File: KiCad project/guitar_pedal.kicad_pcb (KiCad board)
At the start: 2 copper layers, 7 parts, among them J1 NMJ6HCD2, J2 NMJ6HCD2, J3 AVR-ISP-6, SW2 SWITCH_3PDT, U1 ATmega1284-P, U2 L7805

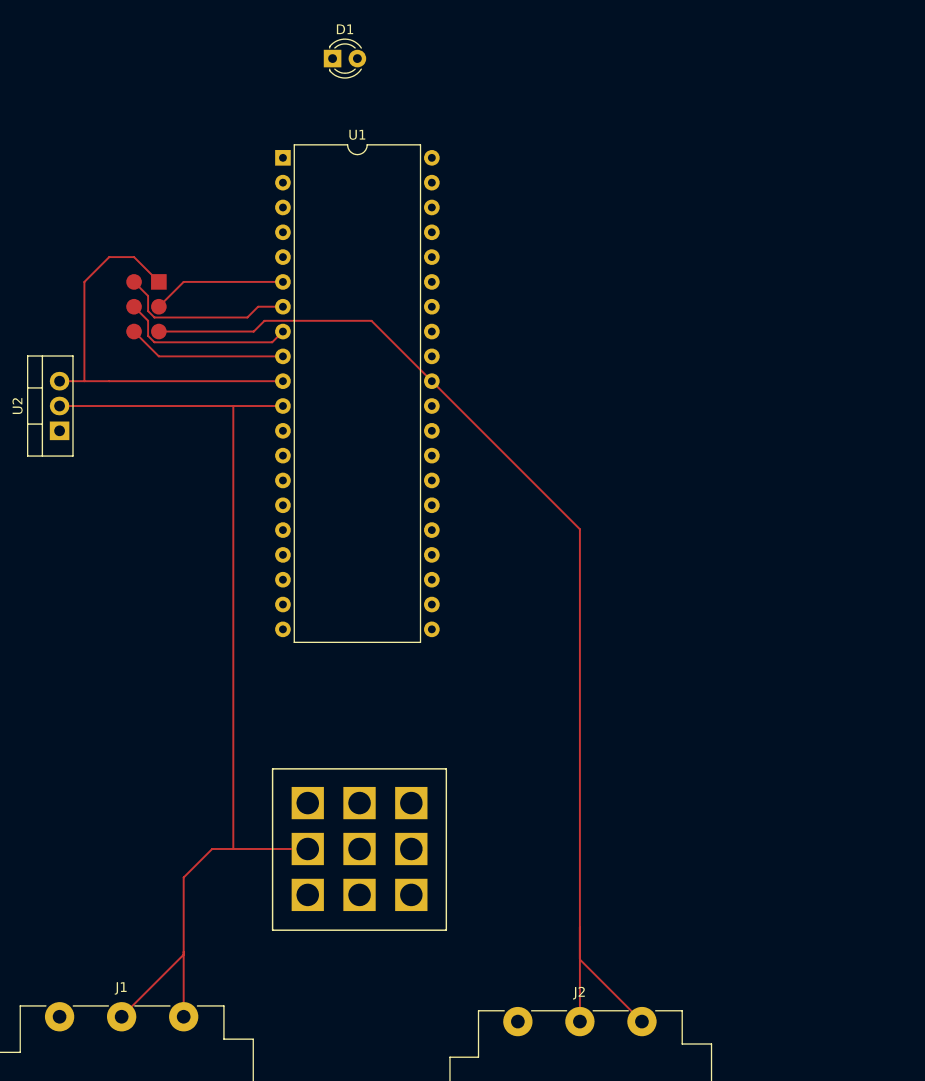
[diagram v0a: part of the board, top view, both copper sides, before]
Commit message: Updated components with footprints, added to PCB
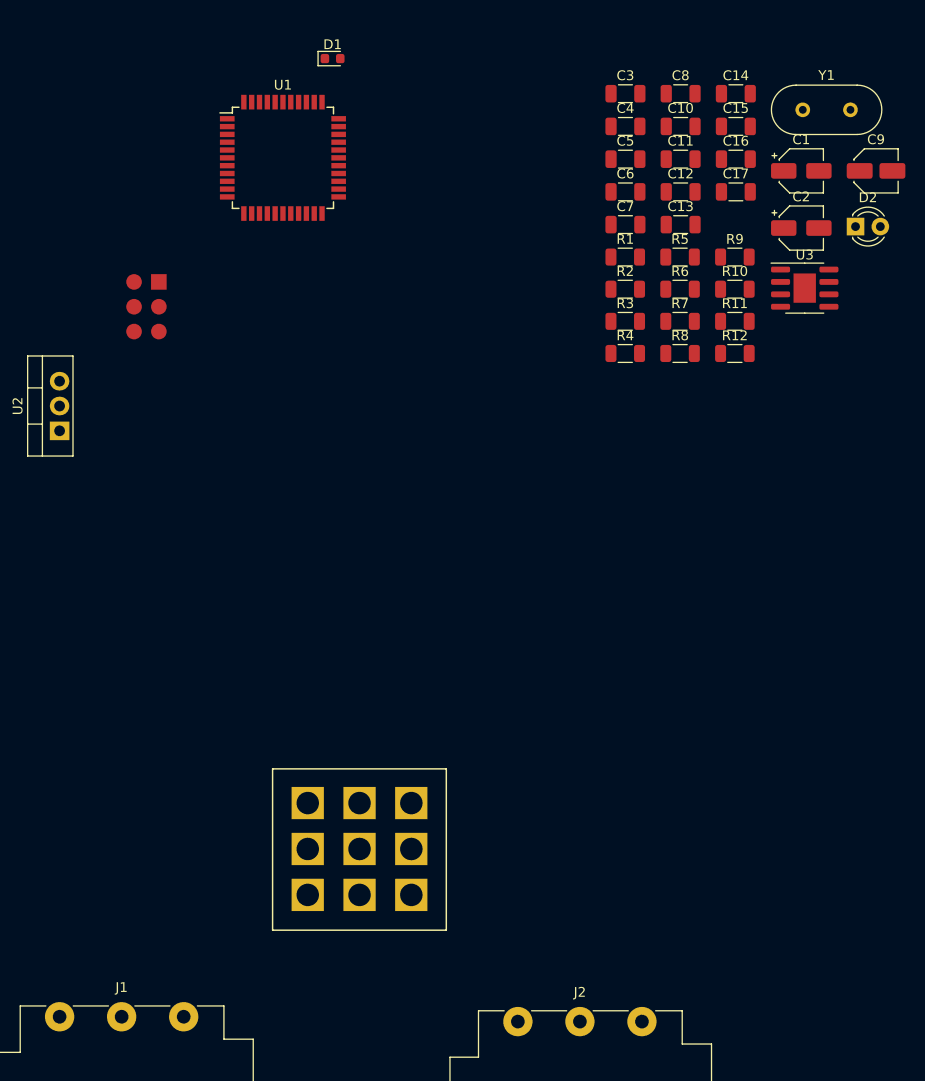
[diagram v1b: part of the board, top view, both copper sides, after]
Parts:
- added C1: 10u, Capacitor_SMD:CP_Elec_4x5.4, F.Cu at (103.9, 44.5)
- added C10: 6.8n, Capacitor_SMD:C_1206_3216Metric, F.Cu at (91.5, 40.0)
- added C11: 6.8n, Capacitor_SMD:C_1206_3216Metric, F.Cu at (91.5, 43.3)
- added C12: 6.8n, Capacitor_SMD:C_1206_3216Metric, F.Cu at (91.5, 46.7)
- added C13: 100n, Capacitor_SMD:C_1206_3216Metric, F.Cu at (91.5, 50.0)
- added C14: 6.8n, Capacitor_SMD:C_1206_3216Metric, F.Cu at (97.2, 36.6)
- added C15: 0.1u, Capacitor_SMD:C_1206_3216Metric, F.Cu at (97.2, 40.0)
- added C16: 0.1u, Capacitor_SMD:C_1206_3216Metric, F.Cu at (97.2, 43.3)
- added C17: 0.1u, Capacitor_SMD:C_1206_3216Metric, F.Cu at (97.2, 46.7)
- added C2: 10u, Capacitor_SMD:CP_Elec_4x5.4, F.Cu at (103.9, 50.4)
- added C3: 0.33u, Capacitor_SMD:C_1206_3216Metric, F.Cu at (85.9, 36.6)
- added C4: 0.1u, Capacitor_SMD:C_1206_3216Metric, F.Cu at (85.9, 40.0)
- added C5: 22p, Capacitor_SMD:C_1206_3216Metric, F.Cu at (85.9, 43.3)
- added C6: 22p, Capacitor_SMD:C_1206_3216Metric, F.Cu at (85.9, 46.7)
- added C7: 0.1u, Capacitor_SMD:C_1206_3216Metric, F.Cu at (85.9, 50.0)
- added C8: 270p, Capacitor_SMD:C_1206_3216Metric, F.Cu at (91.5, 36.6)
- added C9: 1u, Capacitor_SMD:C_Elec_4x5.4, F.Cu at (111.5, 44.5)
- added D2: GREEN LED, LED_THT:LED_D3.0mm, F.Cu at (109.4, 50.2)
- added R1: 330, Resistor_SMD:R_1206_3216Metric, F.Cu at (85.8, 53.3)
- added R10: 4.7k, Resistor_SMD:R_1206_3216Metric, F.Cu at (97.1, 56.6)
- added R11: 120, Resistor_SMD:R_1206_3216Metric, F.Cu at (97.1, 59.9)
- added R12: 10K, Resistor_SMD:R_1206_3216Metric, F.Cu at (97.1, 63.2)
- added R2: 100K, Resistor_SMD:R_1206_3216Metric, F.Cu at (85.8, 56.6)
- added R3: 4.7K, Resistor_SMD:R_1206_3216Metric, F.Cu at (85.8, 59.9)
- added R4: 1M, Resistor_SMD:R_1206_3216Metric, F.Cu at (85.8, 63.2)
- added R5: 18K, Resistor_SMD:R_1206_3216Metric, F.Cu at (91.4, 53.3)
- added R6: 1M, Resistor_SMD:R_1206_3216Metric, F.Cu at (91.4, 56.6)
- added R7: 4.7k, Resistor_SMD:R_1206_3216Metric, F.Cu at (91.4, 59.9)
- added R8: 1M2, Resistor_SMD:R_1206_3216Metric, F.Cu at (91.4, 63.2)
- added R9: 4.7k, Resistor_SMD:R_1206_3216Metric, F.Cu at (97.1, 53.3)
- added U3: TL061, Package_SO:SOIC-8-1EP_3.9x4.9mm_P1.27mm_EP2.29x3mm, F.Cu at (104.2, 56.5)
- added Y1: Crystal 16MHz, Crystal:Crystal_HC49-U_Vertical, F.Cu at (104.0, 38.3)
- D1: footprint LED_THT:LED_D3.0mm -> LED_SMD:LED_0603_1608Metric
- U1: footprint Package_DIP:DIP-40_W15.24mm -> Package_QFP:TQFP-44_10x10mm_P0.8mm
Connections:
- net Net-(U1-PA1) renamed PA1
- SW2 pad 1: Net-(C7-Pad2) -> FX In
- U1 pad 15: Net-(U1-PD1) -> PD1
- U1 pad 16: Net-(U1-PD2) -> PD2
- U1 pad 32: unconnected-(U1-AREF-Pad32) -> Net-(U1-AREF)
- U1 pad 40: Net-(U1-PA0) -> PA0
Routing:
- net GND: track 221.2 -> 0.00 mm
- net +5V: track 42.7 -> 0.00 mm
- net Net-(J3-SCK): track 18.1 -> 0.00 mm
- net Net-(J3-MISO): track 18.1 -> 0.00 mm
- net Net-(J3-~{RST}): track 16.3 -> 0.00 mm
- net Net-(J3-MOSI): track 13.8 -> 0.00 mm

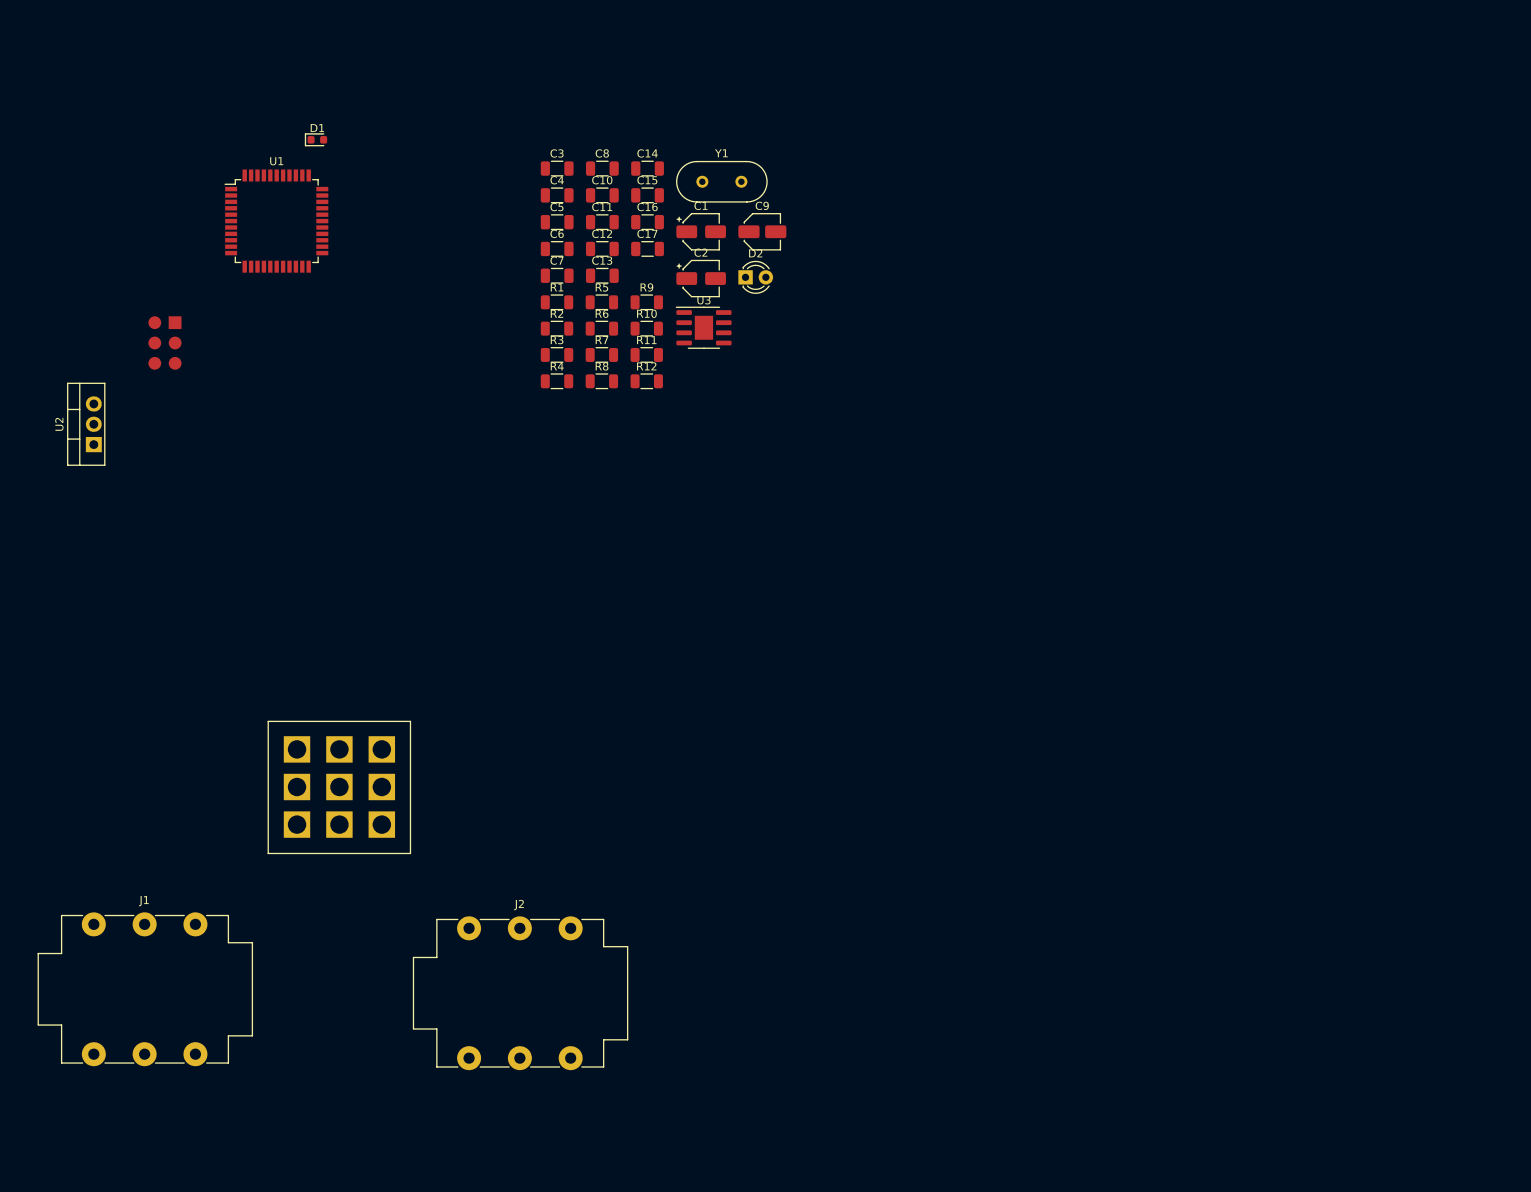
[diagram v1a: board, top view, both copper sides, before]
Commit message: Added traces to power supply and AVR modules in PCB.
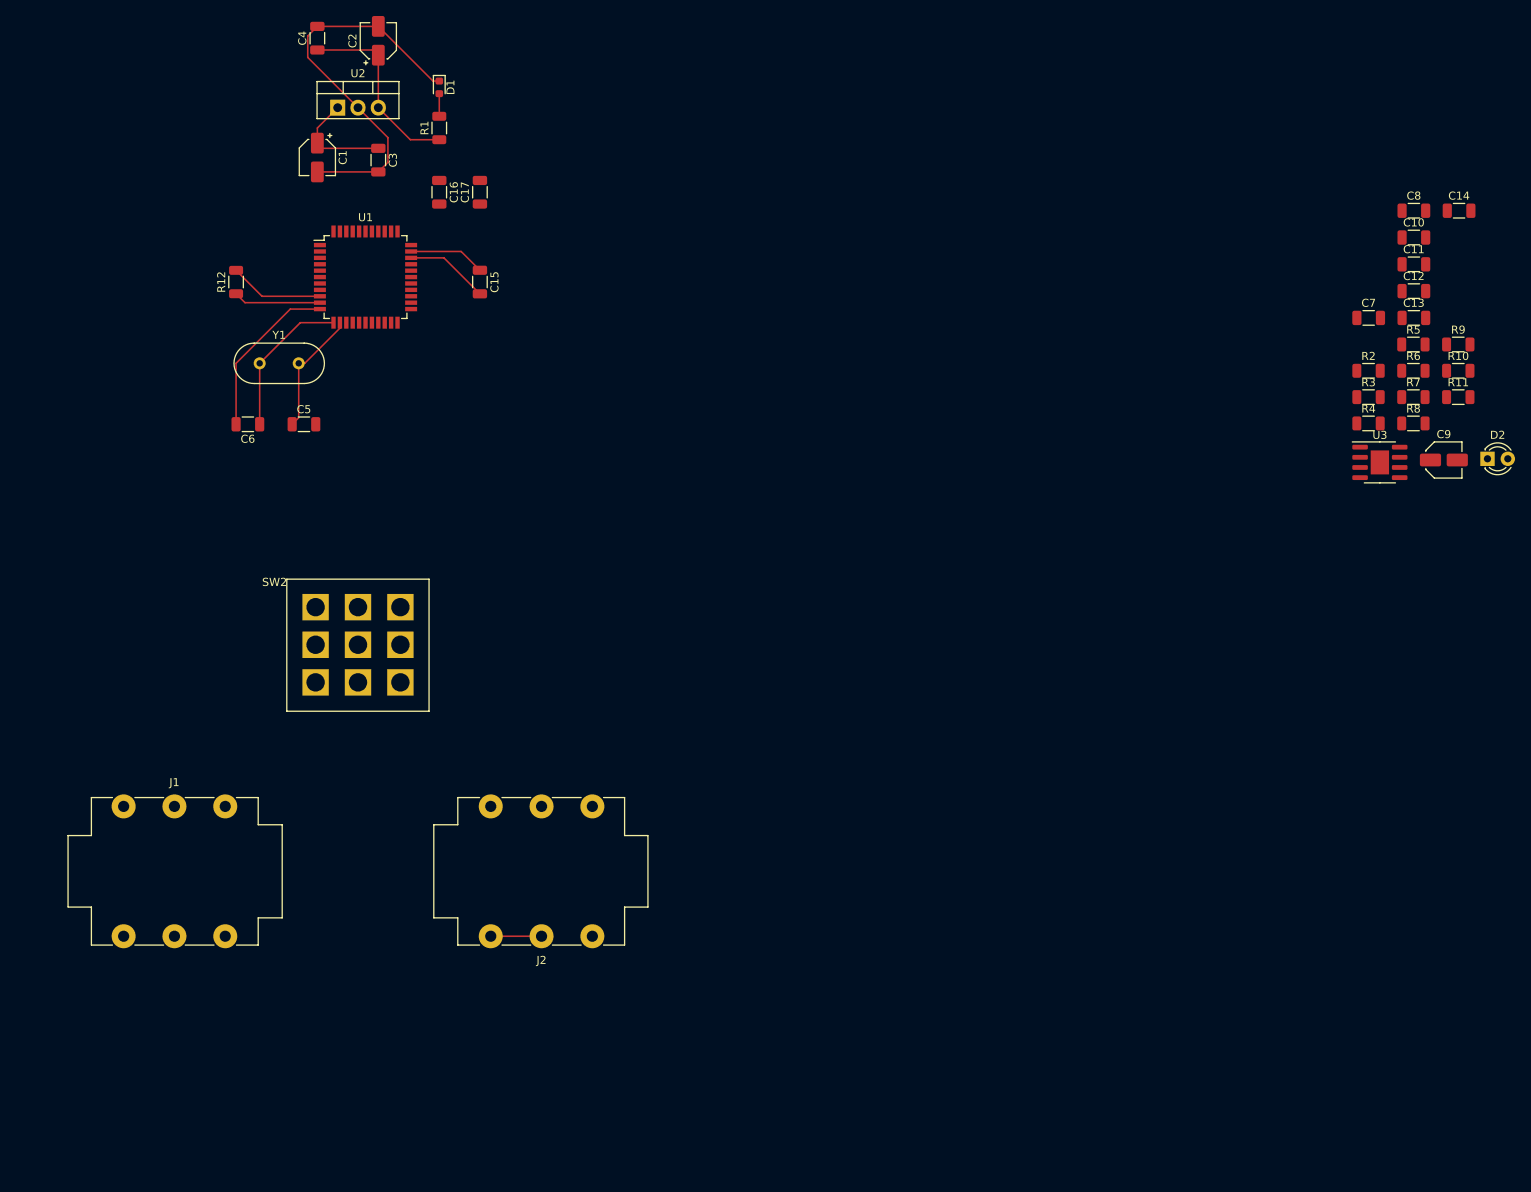
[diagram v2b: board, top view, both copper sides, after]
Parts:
- removed J3: AVR-ISP-6, User:AVR-ISP-6
- moved R2 101.6 mm to (187.3, 61.9)
- moved R3 101.6 mm to (187.3, 65.2)
- moved R4 101.6 mm to (187.3, 68.5)
- moved C10 101.6 mm to (192.9, 45.2)
- moved C11 101.6 mm to (192.9, 48.6)
- moved C12 101.6 mm to (192.9, 51.9)
- moved C13 101.6 mm to (192.9, 55.3)
- moved C14 101.6 mm to (198.6, 41.9)
- moved C8 101.6 mm to (192.9, 41.9)
- moved R10 101.6 mm to (198.5, 61.9)
- moved R11 101.6 mm to (198.5, 65.2)
- moved R5 101.6 mm to (192.9, 58.6)
- moved R6 101.6 mm to (192.9, 61.9)
- moved R7 101.6 mm to (192.9, 65.2)
- moved R8 101.6 mm to (192.9, 68.5)
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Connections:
- J1 pad T: Net-(J1-PadT) -> Net-(SW2-A2)
- J2 pad T: Net-(J2-PadT) -> Net-(SW2-C2)
- SW2 pad 2: GND -> Net-(D2-K)
- SW2 pad 3: Net-(SW2-A-Pad3) -> FX Out
- SW2 pad 4: (no net) -> Net-(SW2-A2)
- SW2 pad 5: (no net) -> GND
- SW2 pad 6: (no net) -> Net-(SW2-C2)
- SW2 pad 7: (no net) -> Net-(SW2-A3)
- SW2 pad 8: (no net) -> unconnected-(SW2-B3-Pad8)
- SW2 pad 9: (no net) -> Net-(SW2-A3)
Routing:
- net GND: track 0.00 -> 86.7 mm
- net +5V: track 0.00 -> 34.7 mm
- net Net-(U1-XTAL2): track 0.00 -> 19.5 mm
- net Net-(U1-XTAL1): track 0.00 -> 15.6 mm
- net Net-(SW1-B): track 0.00 -> 13.4 mm
- net Net-(J3-~{RST}): track 0.00 -> 11.8 mm
- net Net-(U1-AREF): track 0.00 -> 9.57 mm
- net Net-(D1-A): track 0.00 -> 2.83 mm

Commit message: Updates to PCB layout, most connections except ground/power added.
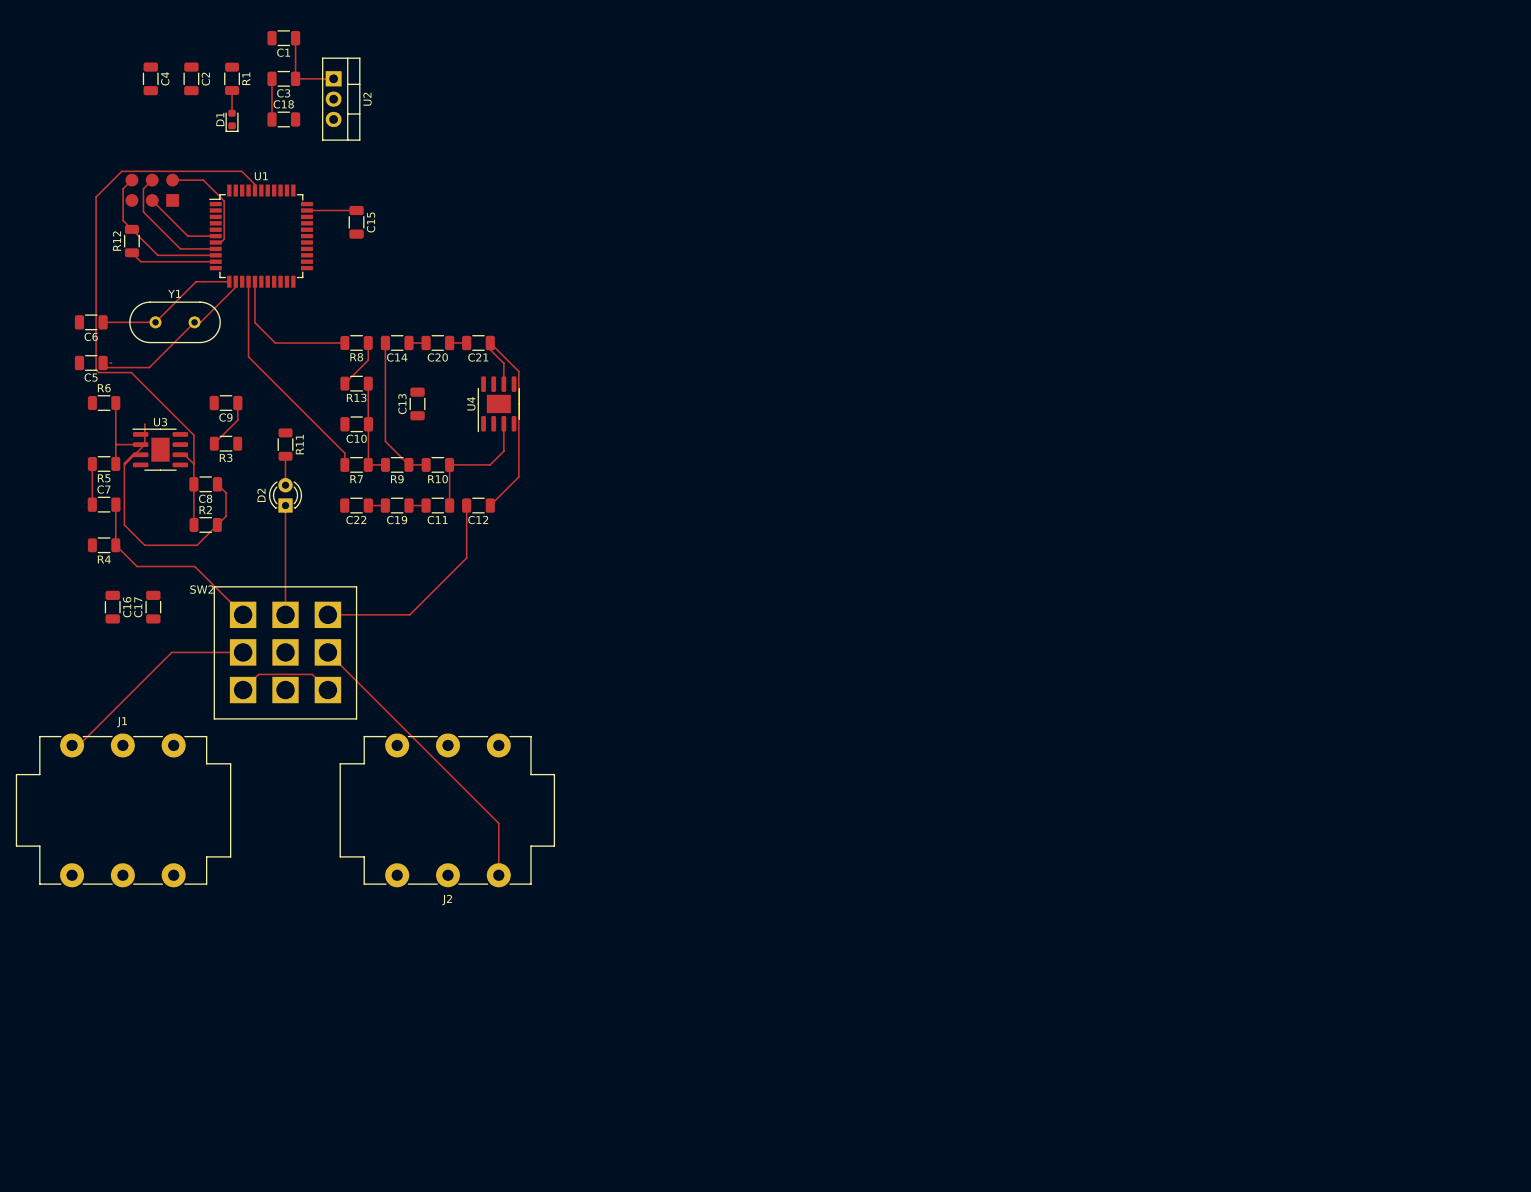
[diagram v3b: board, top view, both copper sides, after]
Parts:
- added C18: 100n, Capacitor_SMD:C_1206_3216Metric, F.Cu at (51.7, 30.5)
- added C19: 2.2n, Capacitor_SMD:C_1206_3216Metric, F.Cu at (65.9, 78.7)
- added C20: 2.2n, Capacitor_SMD:C_1206_3216Metric, F.Cu at (70.9, 58.4)
- added C21: 2.2n, Capacitor_SMD:C_1206_3216Metric, F.Cu at (76.0, 58.4)
- added C22: 2.2n, Capacitor_SMD:C_1206_3216Metric, F.Cu at (60.8, 78.7)
- added J3: AVR-ISP-6, User:AVR-ISP-6, F.Cu at (37.8, 38.1)
- added R13: 200k, Resistor_SMD:R_1206_3216Metric, F.Cu at (60.8, 63.5)
- added U4: TL061, Package_SO:SOIC-8-1EP_3.9x4.9mm_P1.27mm_EP2.29x3mm, F.Cu at (78.6, 66.0)
- C1, C2: footprint Capacitor_SMD:CP_Elec_4x5.4 -> Capacitor_SMD:C_1206_3216Metric
- C11, C14: value 6.8n -> 2.2n
- C12: value 6.8n -> 10n
- C15, C16, C17, C4, C7: value 0.1u -> 100n
- C3: value 0.33u -> 220n
- C8: value 270p -> 330p
- C9: footprint Capacitor_SMD:C_Elec_4x5.4 -> Capacitor_SMD:C_1206_3216Metric
- R8: value 1M2 -> 1M
- moved R5 164.3 mm to (29.2, 73.5), turned to 180 degrees
- moved R6 163.7 mm to (29.2, 65.9)
- moved C7 159.8 mm to (29.2, 78.6)
- moved R4 158.8 mm to (29.2, 83.7), turned to 180 degrees
- moved C8 154.8 mm to (41.9, 76.1), turned to 180 degrees
- moved U3 152.4 mm to (36.3, 71.8)
- moved C9 152.4 mm to (44.5, 65.9), turned to 180 degrees
- moved D2 150.4 mm to (51.9, 78.7), turned to 90 degrees
- moved R11 146.7 mm to (51.9, 71.1), turned to -90 degrees
- moved R2 146.6 mm to (41.9, 81.2)
- moved R3 142.9 mm to (44.5, 71.0), turned to 180 degrees
- moved C10 134.2 mm to (60.8, 68.6), turned to 180 degrees
- moved C14 133.8 mm to (65.9, 58.4), turned to 180 degrees
- moved R9 133.5 mm to (65.9, 73.7), turned to 180 degrees
- moved R8 132.5 mm to (60.8, 58.4), turned to 180 degrees
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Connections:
- C11 pad 2: GND -> Net-(C11-Pad2)
- C14 pad 1: Net-(U4--) -> Net-(C14-Pad1)
- C3 pad 2: GND -> Net-(C18-Pad1)
- R8 pad 1: Net-(C10-Pad1) -> Net-(R13-Pad2)
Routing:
- net GND: track 86.7 -> 0.00 mm
- net PA0: track 0.00 -> 73.3 mm
- net Net-(SW2-C2): track 0.00 -> 38.0 mm
- net Net-(U3-+): track 0.00 -> 36.0 mm
- net Net-(U4--): track 0.00 -> 29.1 mm
- net PD1: track 0.00 -> 27.9 mm
- net FX Out: track 0.00 -> 26.8 mm
- net Net-(SW2-A2): track 0.00 -> 26.2 mm
- net FX In: track 0.00 -> 24.6 mm
- net +5V: track 34.7 -> 10.9 mm
- net Net-(C14-Pad2): track 0.00 -> 18.6 mm
- net PD2: track 0.00 -> 17.4 mm
- net Net-(U4-+): track 0.00 -> 16.0 mm
- net Net-(J3-SCK): track 0.00 -> 15.4 mm
- net Net-(D2-K): track 0.00 -> 13.7 mm
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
